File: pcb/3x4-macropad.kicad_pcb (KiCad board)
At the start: 2 copper layers, 83.1 x 78.9 mm, 54 parts, among them SW1 SW_Push, SW10 SW_Push, SW11 SW_Push, SW12 SW_Push, SW2 SW_Push, SW3 SW_Push, SW4 SW_Push, SW5 SW_Push, SW6 SW_Push, SW7 SW_Push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

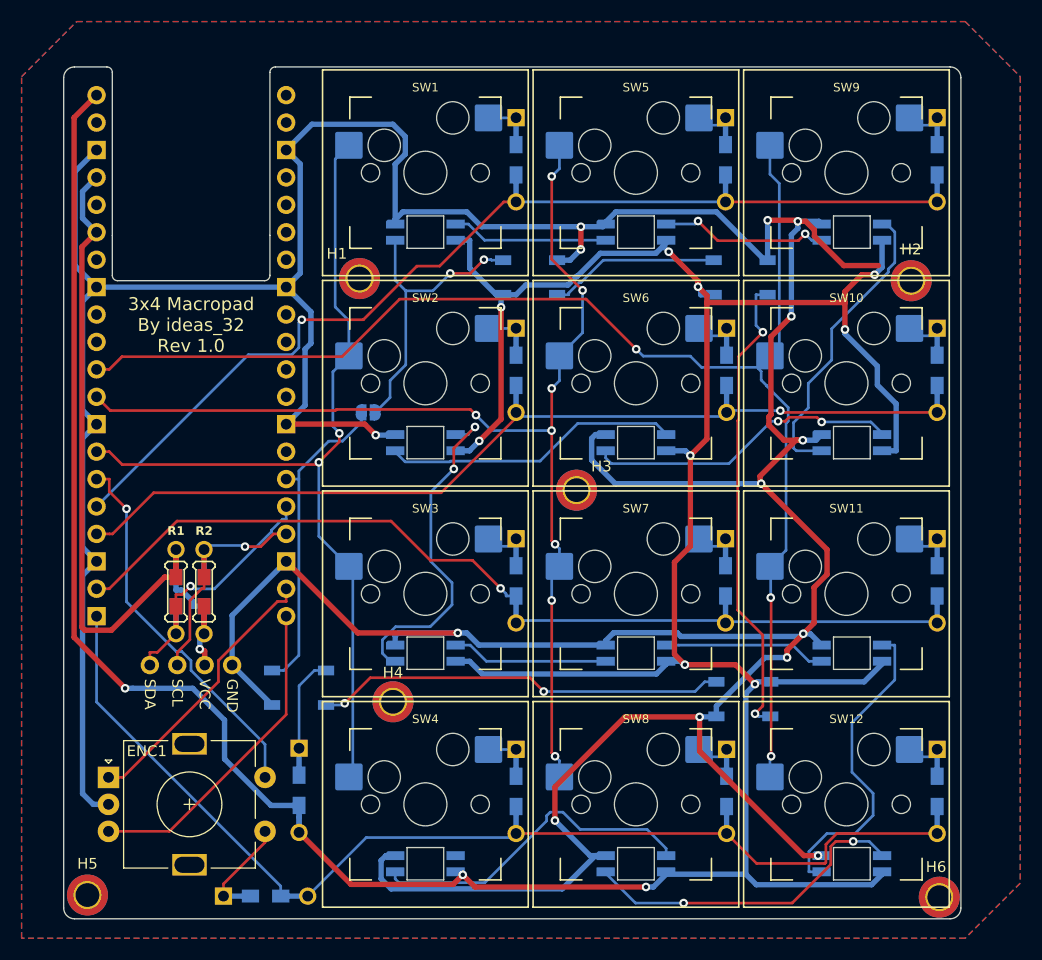
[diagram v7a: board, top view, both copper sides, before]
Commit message: Removed zone that made ground pads hard to solder
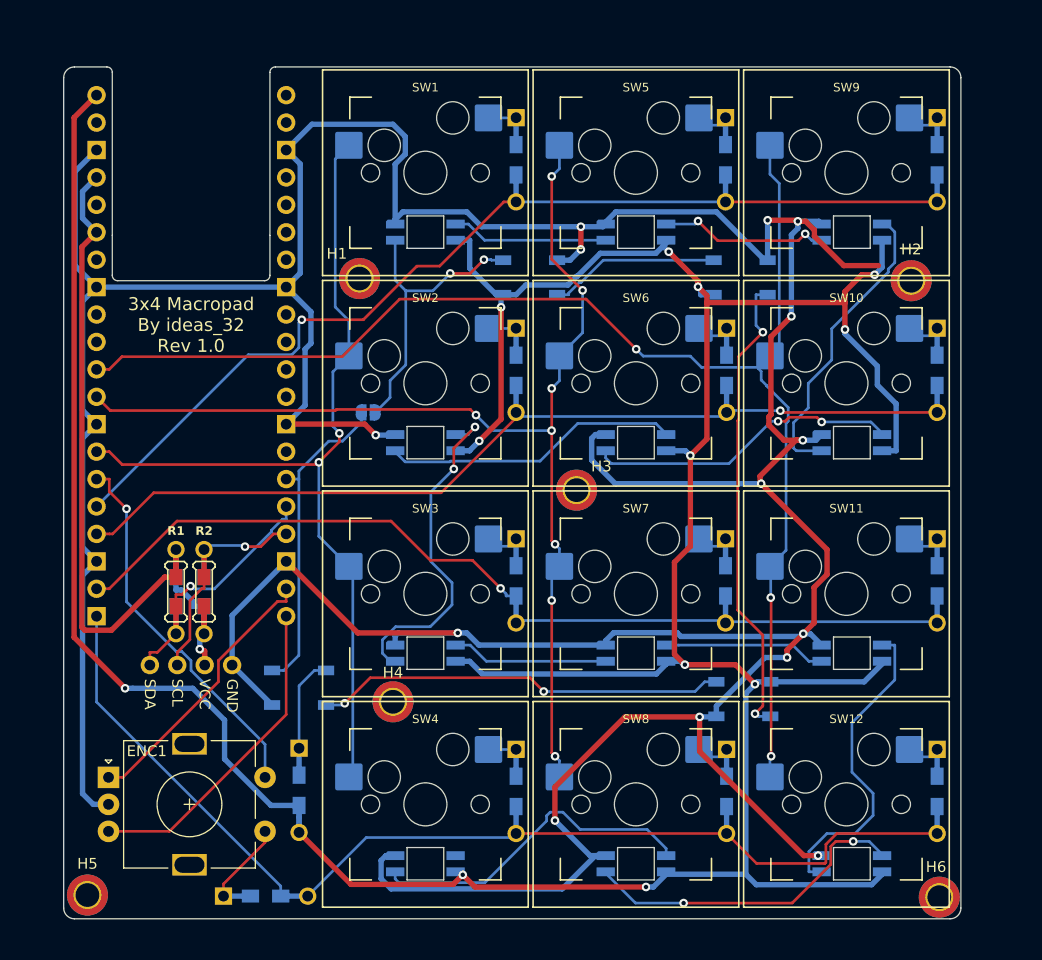
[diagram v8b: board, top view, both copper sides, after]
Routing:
- removed copper zone on B.Cu, net GND
- removed copper zone on F.Cu, net GND
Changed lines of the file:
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@@
   (segment (start 149.3 96.8) (end 149.3 95.7) (width 0.25) (layer "B.Cu") (net 62))
   (segment (start 149.3 94.3) (end 149.3 88.5217) (width 0.25) (layer "B.Cu") (net 62))
-  (zone (net 17) (net_name "GND") (layers "F&B.Cu") (name "GND") (hatch edge 0.5)
-    (connect_pads yes (clearance 0.5))
-    (min_thickness 0.25) (filled_areas_thickness no)
-    (fill yes (thermal_gap 0.5) (thermal_bridge_width 0.5) (smoothing fillet))
-    (polygon
-      (pts
-        (xy 211 111.9)
-        (xy 123.6 111.9)
-        (xy 123.6 32.1)
-        (xy 128.7 27)
-        (xy 211 27)
-        (xy 216.1 32.1)
-        (xy 216.1 106.8)
-      )
-    )
-  )
 )
